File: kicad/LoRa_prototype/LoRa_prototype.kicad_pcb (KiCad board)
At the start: 4 copper layers, 100 x 90 mm, 142 parts, among them J1 Conn_ST_STDC14, J10 SYS, J11 BME, J12 GPS, J14 SPI_FLASH, J15 SYS, J18 MCO, J2 USB_C_Receptacle_PowerOnly_6P, J3 BAT, J4 SMA Female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

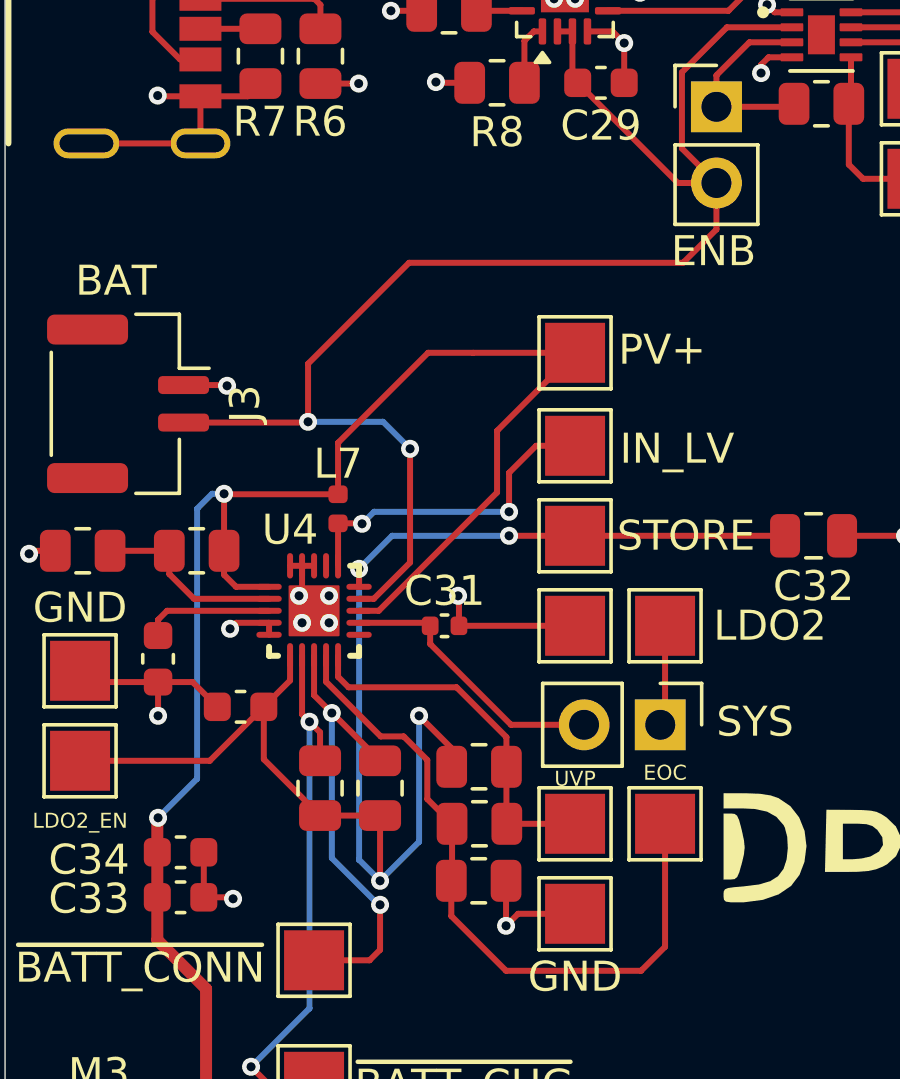
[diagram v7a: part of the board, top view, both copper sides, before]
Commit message: Changed L7 to power inductor
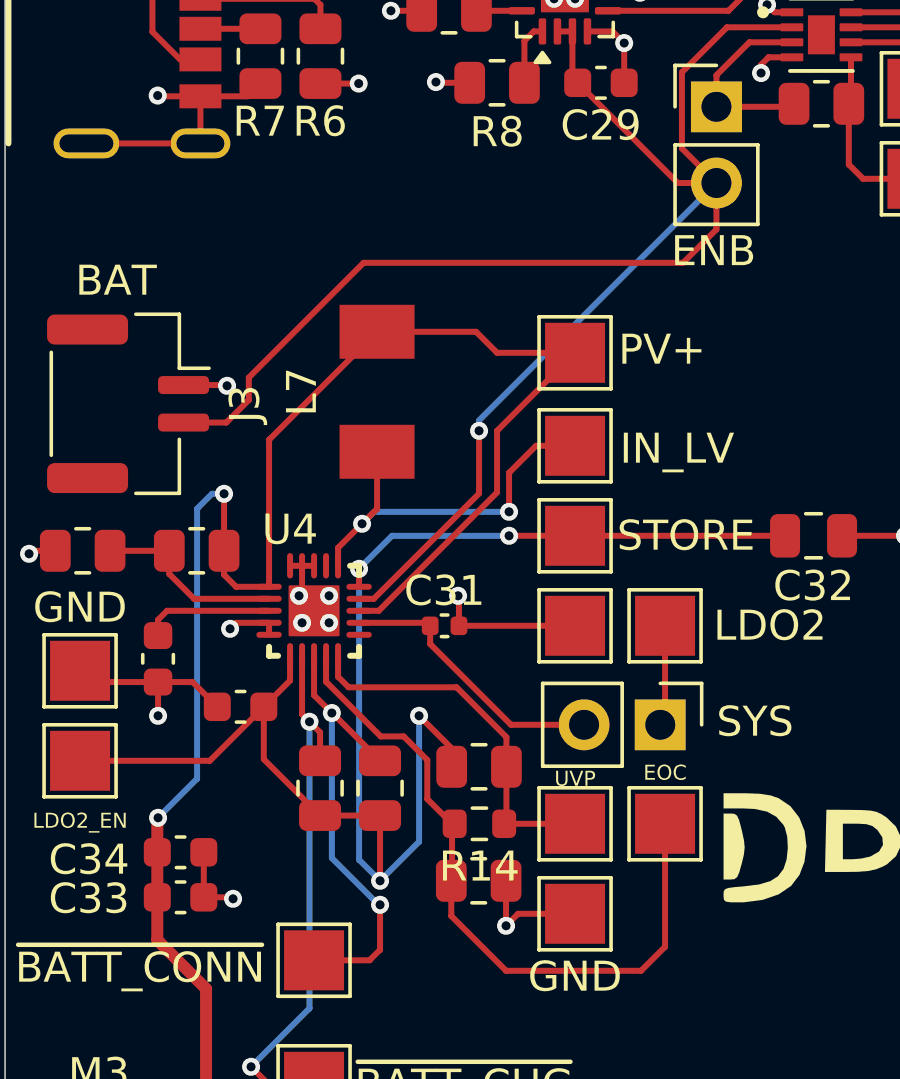
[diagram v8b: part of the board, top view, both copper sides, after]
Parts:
- L7: footprint Inductor_SMD:L_0402_1005Metric -> footprints:PSPMAA0402-220M-ANP
- R14: footprint Resistor_SMD:R_0805_2012Metric -> Resistor_SMD:R_0603_1608Metric
- moved L7 4.11 mm to (101.4, 94.7)
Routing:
- net /POWER/BAT+: track 49.5 -> 58.2 mm, vias 2 -> 1
- net /POWER/MPP: track 75.5 -> 77.8 mm
- net Net-(U4-IN_LV): track 11.2 -> 13.3 mm
